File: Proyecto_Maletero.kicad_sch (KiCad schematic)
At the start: 42 parts, among them J1 DE9_Pins, J2 Conn_01x02, J3 Conn_01x02, J4 Conn_01x03, J5 Conn_01x02, J6 DE9_Pins, J8 Conn_01x02, J9 Conn_01x02, SW1 SW_Push, SW3 SW_SPST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

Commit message: Mas correcciones
Final de carrera, etc.
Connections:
- net Clock_I2C: no longer names the net of U3.14 (RC3/SCK/SCL)
- net I2C: no longer names the net of U3.15 (RC4/SDI/SDA)
- net SENSE: no longer names the net of R10.2, R8.1, R9.1, U4.15 (SENSE_B), U5.1 (+)
- no-connect marks 21 -> 24
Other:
- note removed: "No componentes con I2C"
- note removed: "Refresco de datos I2C"
- moved on the sheet: C15, C6, C7, C8, J2, J8, J9, R1, SW1, SW3, Y1

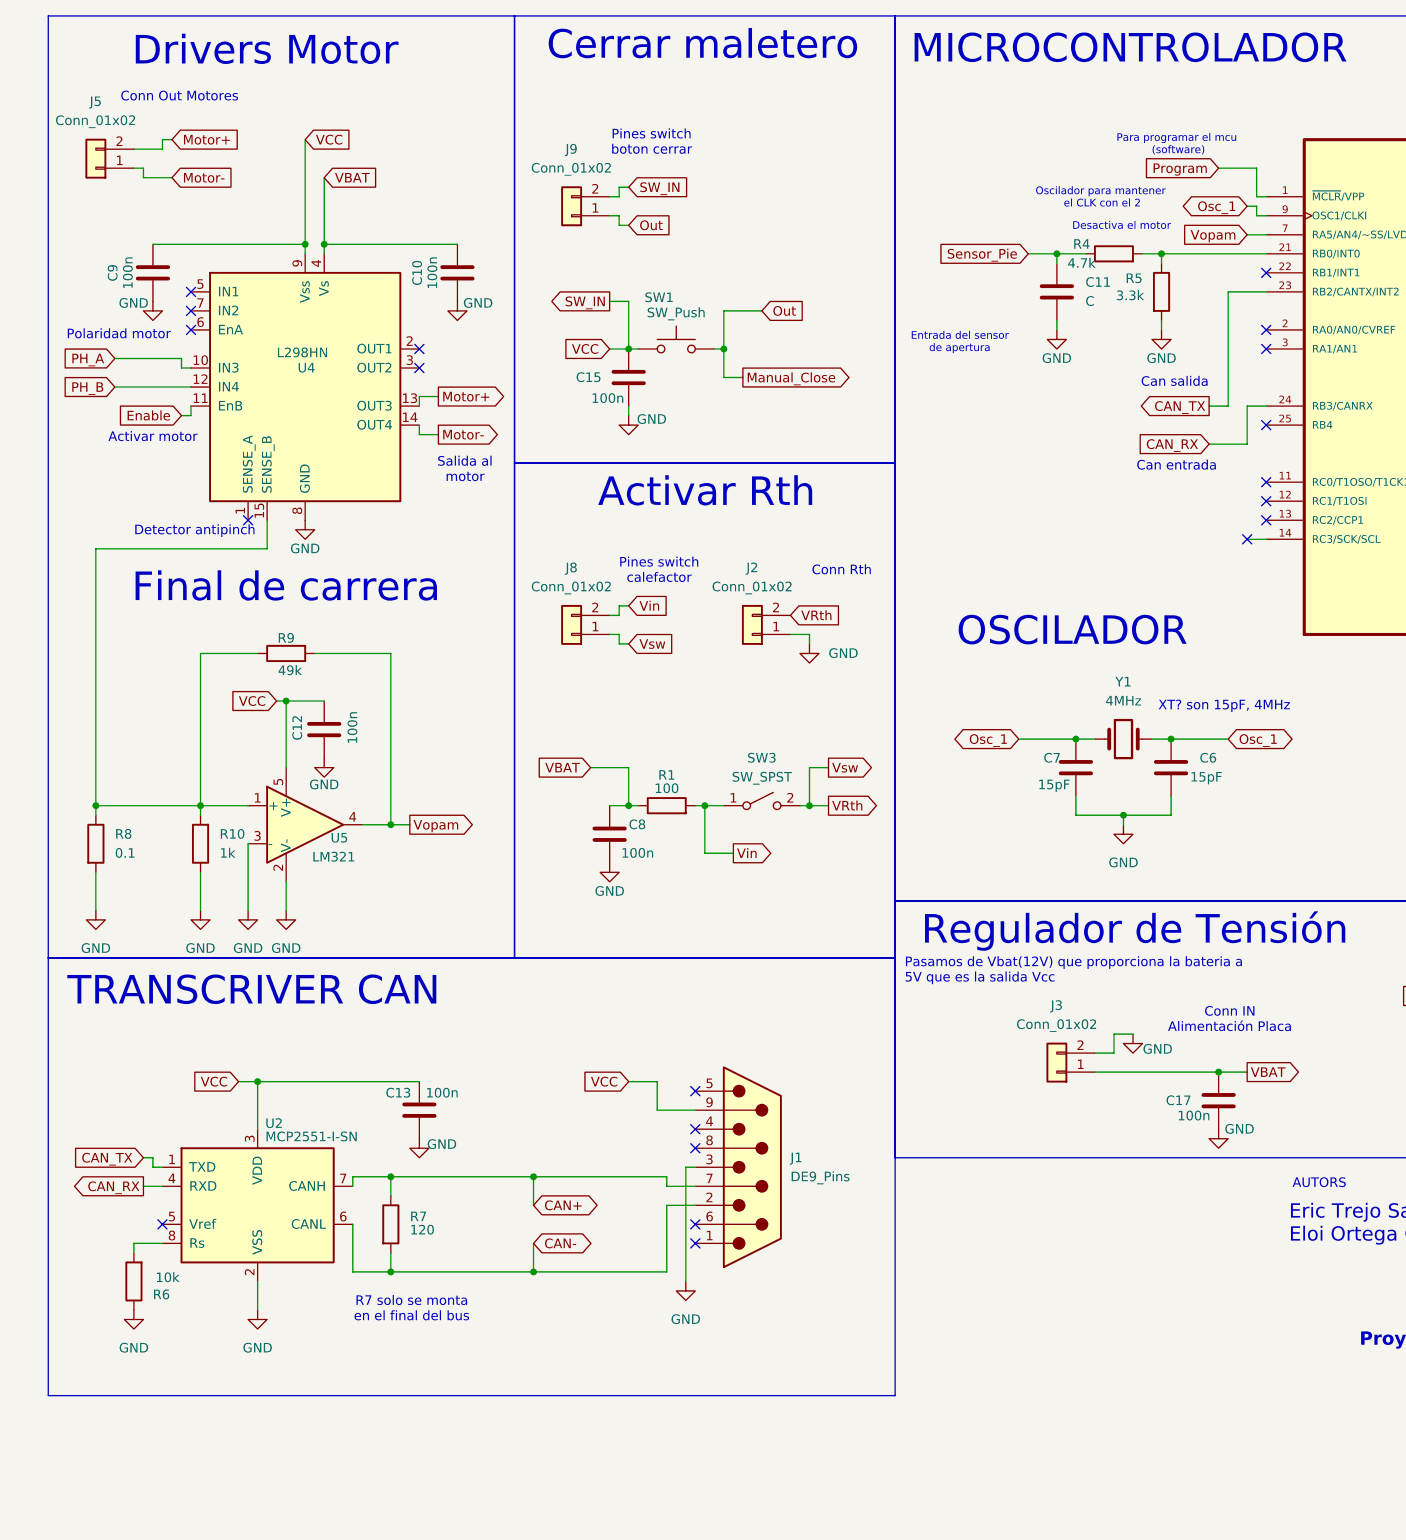
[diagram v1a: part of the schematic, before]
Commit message: Correccion switch y anadido las net list
Hemos anadido un rele y un npn para controlar la Rth
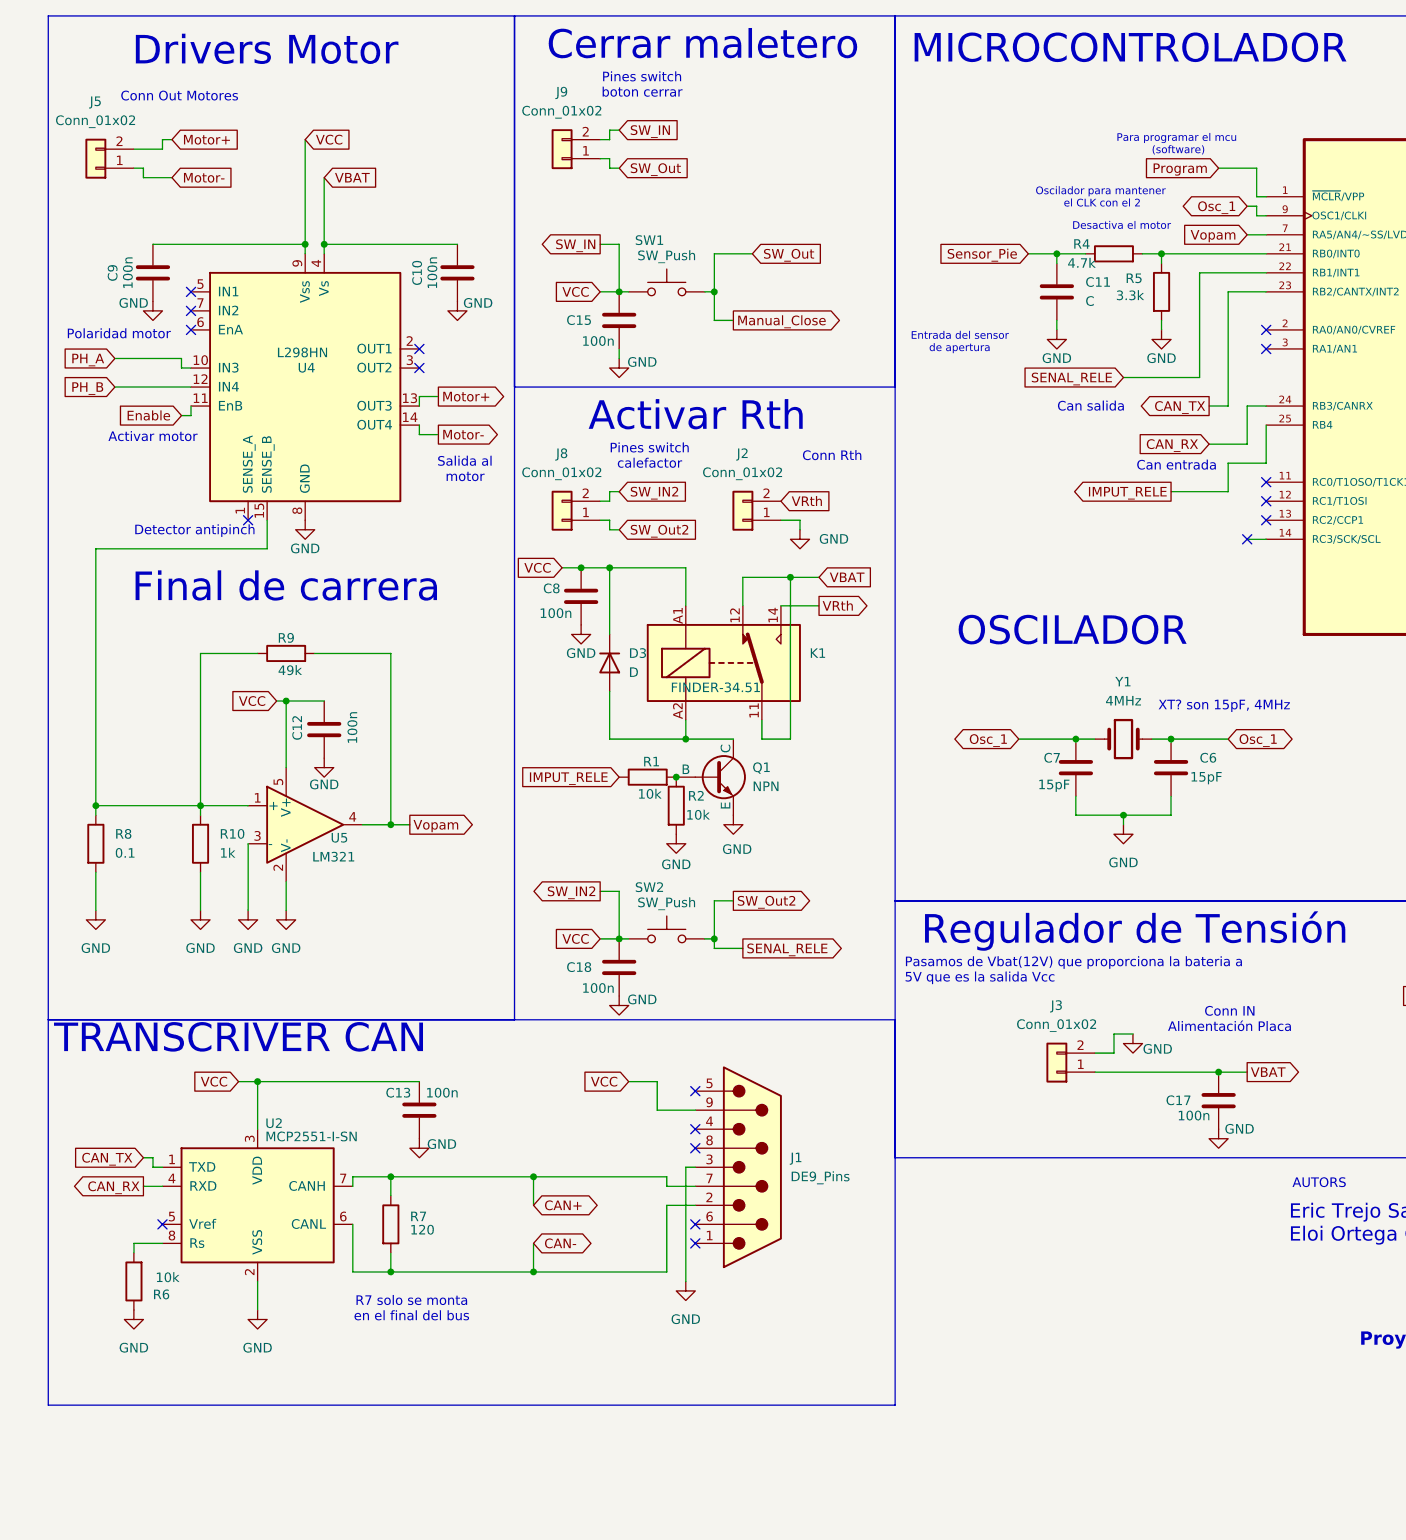
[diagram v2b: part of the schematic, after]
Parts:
- removed SW3: SW_SPST, symbol Switch:SW_SPST
- added C18: 100n, symbol Device:C
- added D3: D, symbol Device:D
- added K1: FINDER-34.51, Relay_THT:Relay_SPDT_Finder_34.51_Vertical, symbol Relay:FINDER-34.51
- added Q1: NPN, symbol Simulation_SPICE:NPN
- added R2: 10k, symbol Device:R
- added SW2: SW_Push, symbol Switch:SW_Push
- R1: value 100 -> 10k
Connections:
- net GND: now also C18.1, Q1.3 (E), R2.2
- net SW_IN: now also C8.1, J8.2 (Pin_2), C18.2, D3.1 (K), K1.A1, SW2.1
- net VBAT: now also K1.11, K1.12; no longer C8.1, R1.1
- net VRth: now also K1.14; no longer J8.1 (Pin_1)
- net SENAL_RELE: now reaches U3.22 (RB1/INT1)
- net SENAL_RELE: now also J8.1 (Pin_1), SW2.2
- net IMPUT_RELE: now reaches U3.25 (RB4)
- net IMPUT_RELE: now also R1.1
- net Vin: no longer names the net of R1.2
- net Vin: now also Q1.2 (B), R2.1; no longer J8.2 (Pin_2)
- new net: D3.2 (A), K1.A2, Q1.1 (C)
- no-connect marks 24 -> 22
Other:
- moved on the sheet: C15, C8, J2, J8, J9, SW1

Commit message: Orden
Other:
- note added: "DE9"
- note added: "SENSOR"
- note removed: "Falta conectar al USB"
- moved on the sheet: C11, C14, C16, C6, C7, J4, J6, R4, R5, U3, Y1

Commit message: Correccion errores
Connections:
- net SENSE: now reaches R10.2, R8.1, R9.1, U4.15 (SENSE_B), U5.1 (+)
- net SW_IN renamed VCC
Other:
- moved on the sheet: C18, SW2

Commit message: Lo mismo pero guardando el proyecto
Solo queda hacer la etapa de regulación del sensor y entramos al layout
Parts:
- removed C11: C, symbol Device:C
- removed R4: 4.7k, symbol Device:R
- removed R5: 3.3k, symbol Device:R
- added C3: C, symbol Device:C
- added U6: LM1084-5.0, symbol Regulator_Linear:LM1084-5.0
- R7: value 120 -> 60
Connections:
- net CAN+: now also J1.2; no longer J1.7
- net CAN-: now also J1.7; no longer J1.2
- net GND: now also J6.5, C3.2, U6.1 (GND)
- net Sensor_Pie: now also U3.21 (RB0/INT0), C3.1, U6.2 (VO); no longer J4.3 (Pin_3)
- net VCC: no longer J6.9
- net IMPUT_RELE renamed INPUT_RELE
- net Program: no longer names the net of U3.1 (~{MCLR}/VPP)
- net SENSE: no longer names the net of R10.2, R8.1, R9.1, U4.15 (SENSE_B), U5.1 (+)
- new net Sensor_Pie_12V: J4.3 (Pin_3), U6.3 (VI)
- no-connect marks 22 -> 29
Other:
- note added: "15pF, 4MHz"
- note added: "DE-9"
- note added: "Microcontrolador"
- note added: "Oscilador"
- note added: "Sensor"
- note added: "Sensor a 5V"
- note added: "Transcriver CAN"
- note removed: "DE9"
- note removed: "MICROCONTROLADOR"
- note removed: "OSCILADOR"
- note removed: "SENSOR"
- note removed: "TRANSCRIVER CAN"
- note removed: "XT? son 15pF, 4MHz"
- moved on the sheet: J8, Q1, R2

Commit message: auctualizacion y cambio de sensor
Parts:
- removed U4: L298HN, Package_TO_SOT_THT:TO-220-15_P2.54x2.54mm_StaggerOdd_Lead5.84mm_TabDown, symbol Driver_Motor:L298HN
- added U7: DRV8870DDA, Package_SO:Texas_HTSOP-8-1EP_3.9x4.9mm_P1.27mm_EP2.95x4.9mm_Mask2.4x3.1mm_ThermalVias, symbol Driver_Motor:DRV8870DDA
- C3: value C -> 100n
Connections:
- net GND: now also U7.1 (GND), U7.9 (GND)
- net Motor+: now also U7.6 (OUT1)
- net Motor-: now also U7.8 (OUT2)
- net PH_A: now also U7.3 (IN1)
- net PH_B: now also U7.2 (IN2)
- net Sensor_Pie: no longer C3.1
- net Sensor_Pie_12V: now also C3.1
- net SENSE: now reaches R10.2, R8.1, R9.1, U5.1 (+)
- net SENSE: now also U7.7 (ISEN)
- net Enable: no longer names the net of U3.6 (RA4/T0CKI)
- no-connect marks 29 -> 25
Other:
- note removed: "Activa el motor"
- note removed: "Activar motor"
- moved on the sheet: C3

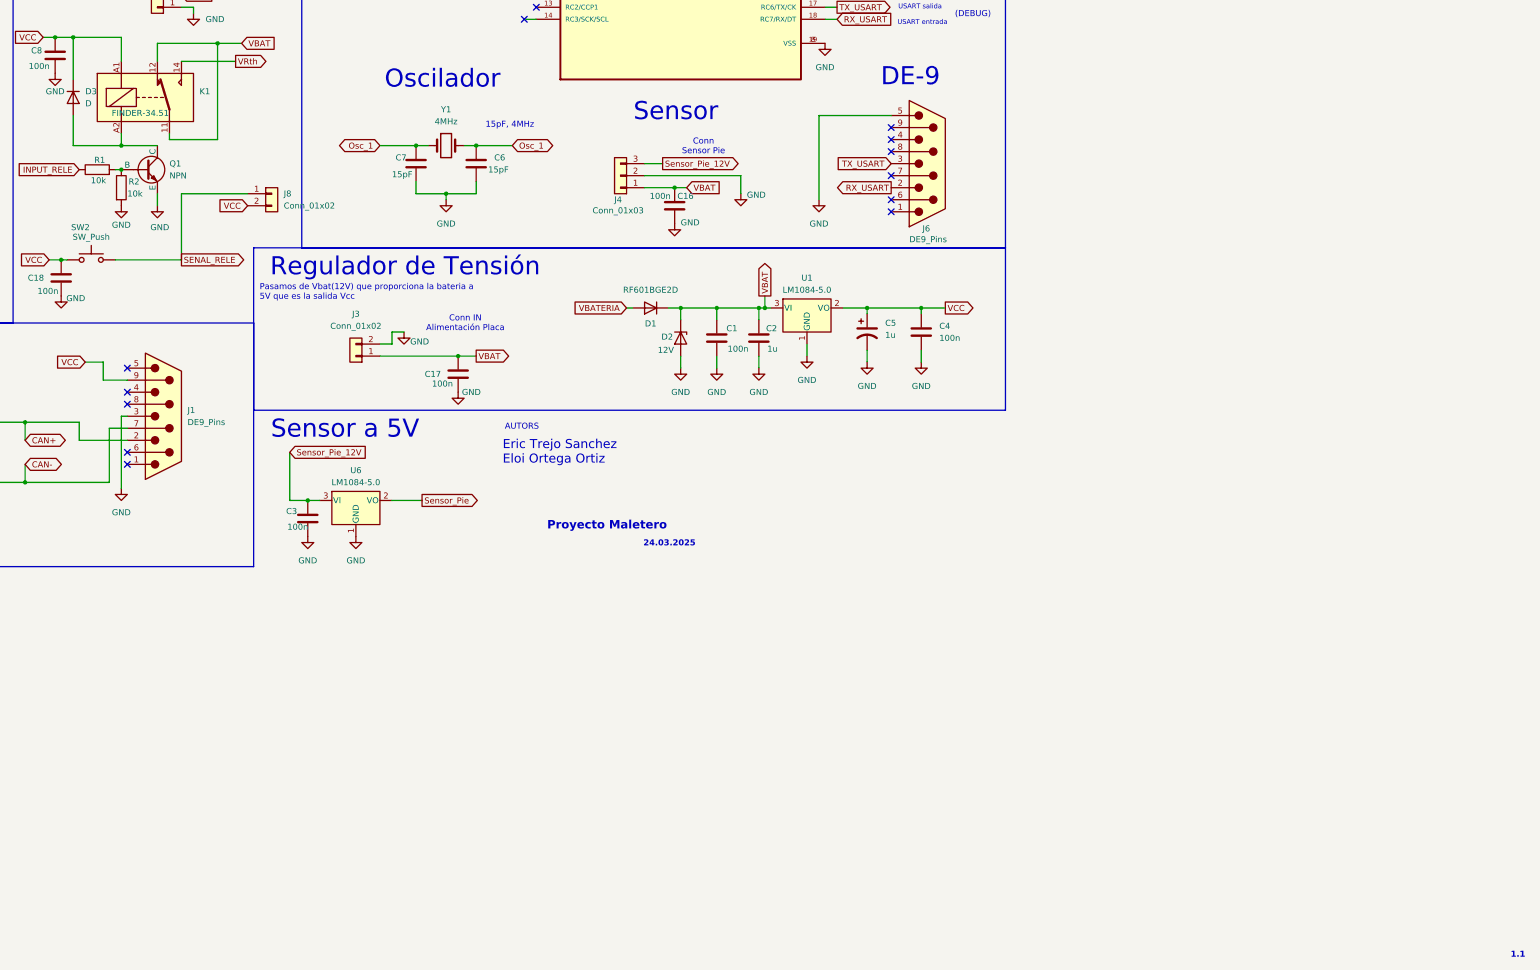
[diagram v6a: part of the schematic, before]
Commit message: Añadido huellas
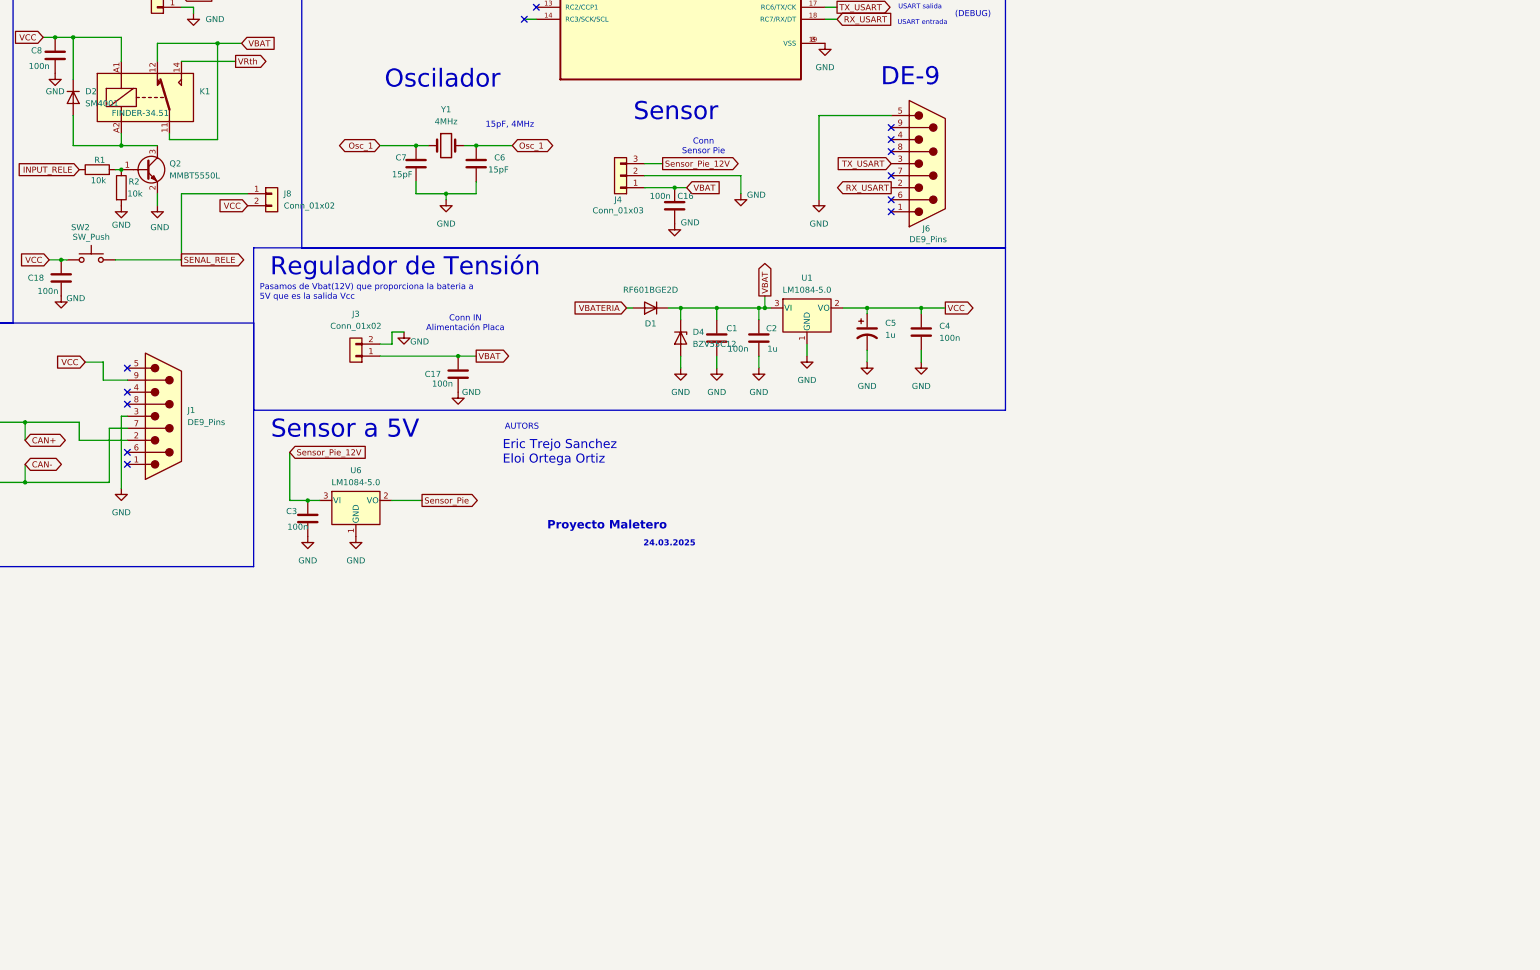
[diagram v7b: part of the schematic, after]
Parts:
- removed D2: 12V, symbol Device:D_Zener
- removed D3: D, symbol Device:D
- removed Q1: NPN, symbol Simulation_SPICE:NPN
- added D2: SM4001, Diode_SMD:D_MELF, symbol Diode:SM4001
- added D4: BZV55C12, Diode_SMD:D_MiniMELF, symbol Diode:BZV55C12
- added Q2: MMBT5550L, Package_TO_SOT_SMD:SOT-23, symbol Transistor_BJT:MMBT5550L
- C1, C10, C12, C13, C14, C15, C16, C17, C18, C2, C3, C4, C5, C6, C7, C8, C9: footprint (none) -> Capacitor_SMD:C_0805_2012Metric
- D1: footprint (none) -> Diode_SMD:D_0805_2012Metric
- J1, J6: footprint (none) -> Connector_PinHeader_2.54mm:PinHeader_1x09_P2.54mm_Vertical
- J2: footprint (none) -> TerminalBlock_Phoenix:TerminalBlock_Phoenix_MKDS-1,5-2-5.08_1x02_P5.08mm_Horizontal
- J4: footprint (none) -> TerminalBlock_Phoenix:TerminalBlock_Phoenix_MKDS-1,5-3_1x03_P5.00mm_Horizontal
- J8, J9: footprint (none) -> TerminalBlock_Phoenix:TerminalBlock_Phoenix_MKDS-1,5-3-5.08_1x03_P5.08mm_Horizontal
- R1, R10, R2, R6, R7, R8, R9: footprint (none) -> Resistor_SMD:R_0805_2012Metric
- SW1, SW2: now left out of the parts list
- U1, U6: footprint (none) -> Library:LT1117
- Y1: footprint (none) -> Crystal:Crystal_SMD_HC49-SD
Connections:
- net GND: now also D4.2 (A), Q2.2 (E)
- net VBAT: now also D4.1 (K)
- net VCC: now also D2.1 (K)
- net at K1.A2: now also D2.2 (A), Q2.3 (C)
- net at R1.2, R2.1: now also Q2.1 (B)
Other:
- note removed: "1.1"

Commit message: Comiezo layaut
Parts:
- U3: footprint PIC18F258-I_SO:SOIC127P1030X265-28N -> PIC18F258-I_SO (1):SOIC127P1030X265-28N
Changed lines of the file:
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@@
 			)
 		)
-		(property "Footprint" "PIC18F258-I_SO:SOIC127P1030X265-28N"
+		(property "Footprint" "PIC18F258-I_SO (1):SOIC127P1030X265-28N"
 			(at 215.9 62.23 0)
 			(effects
